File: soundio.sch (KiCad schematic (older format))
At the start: 13 parts, among them J3 PORT B, J4 PORT B, Q1 2N3904, U13 AY-3-8910, U14 LM741

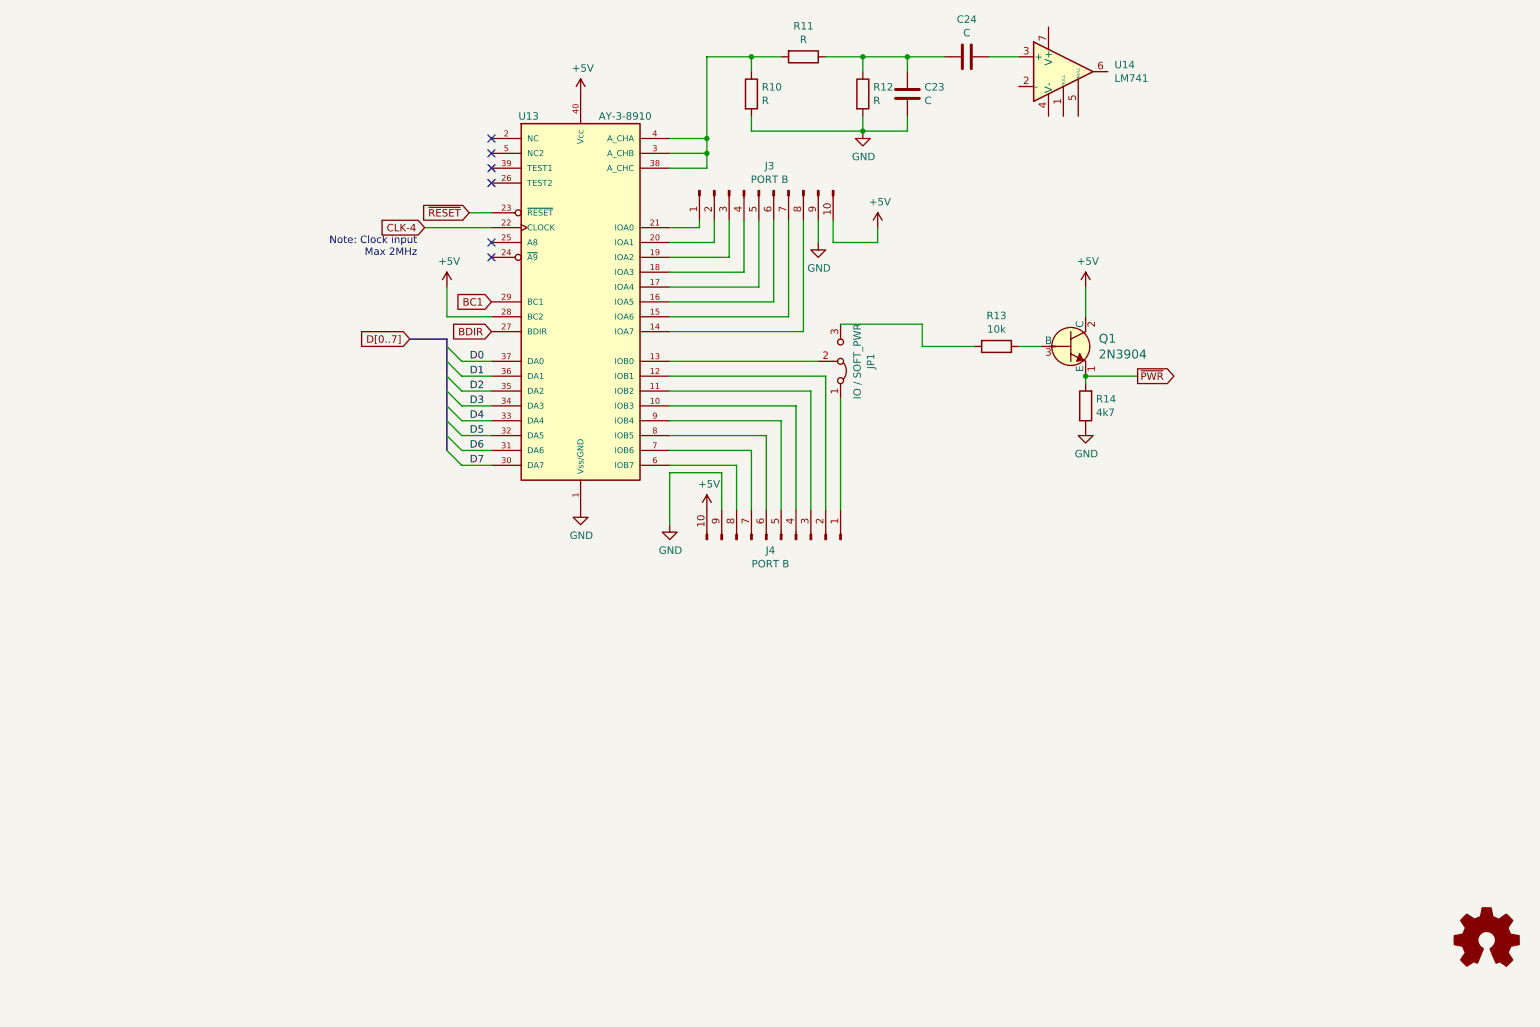
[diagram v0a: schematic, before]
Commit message: Added RTC
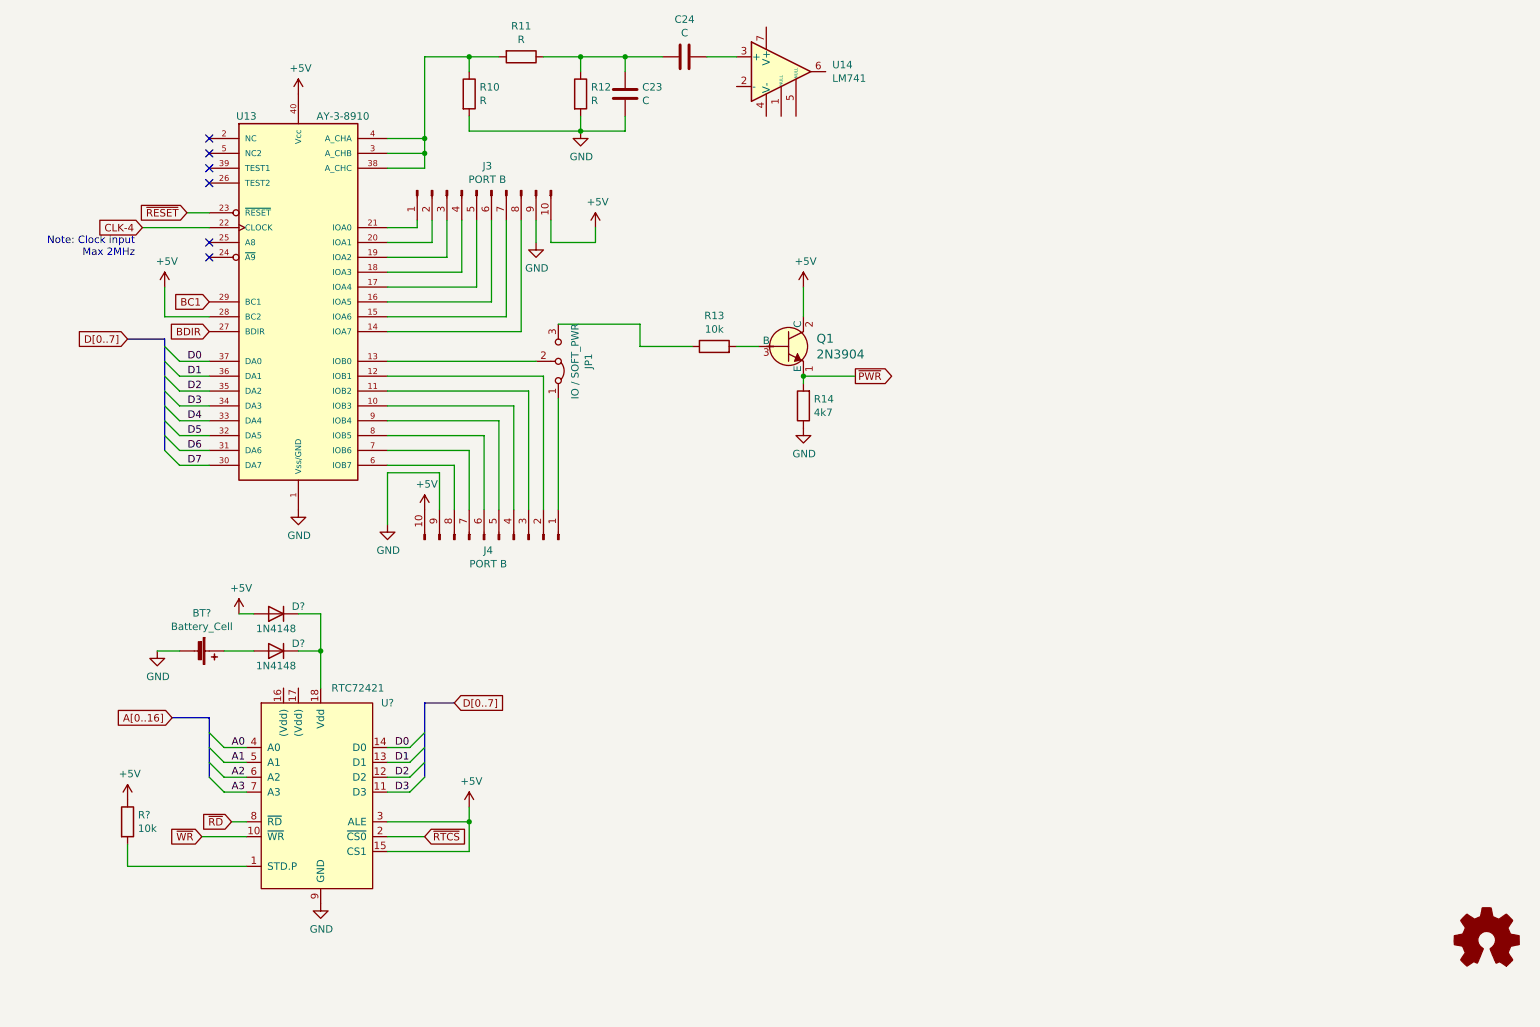
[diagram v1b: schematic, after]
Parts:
- added BT?: Battery_Cell, symbol Device:Battery_Cell
- added D? (x2): 1N4148, Diode_THT:D_DO-35_SOD27_P7.62mm_Horizontal, symbol Diode:1N4148
- added R?: 10k, symbol Device:R
- added U?: RTC72421, Package_DIP:DIP-18_W7.62mm_Socket_LongPads, symbol personal:RTC72421
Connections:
- net +5V: now also D?.2 (A), R?.1, U?.15 (CS1), U?.3 (ALE)
- net D0: now also U?.14 (D0)
- net D1: now also U?.13 (D1)
- net D2: now also U?.12 (D2)
- net D3: now also U?.11 (D3)
- net GND: now also BT?.2 (-), U?.9 (GND)
- new net: R?.2, U?.1 (STD.P)
- new net: D?.1 (K), D?.1 (K), U?.18 (Vdd)
- new net: BT?.1 (+), D?.2 (A)
- new net A0: U?.4 (A0)
- new net A1: U?.5 (A1)
- new net A2: U?.6 (A2)
- new net A3: U?.7 (A3)
- new net ~RD: U?.8 (~RD)
- new net ~RTCS: U?.2 (~CS0)
- new net ~WR: U?.10 (~WR)
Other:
- moved on the sheet: C23, C24, J3, J4, JP1, Q1, R10, R11, R12, R13, R14, U13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

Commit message: Added PSG audio output stage
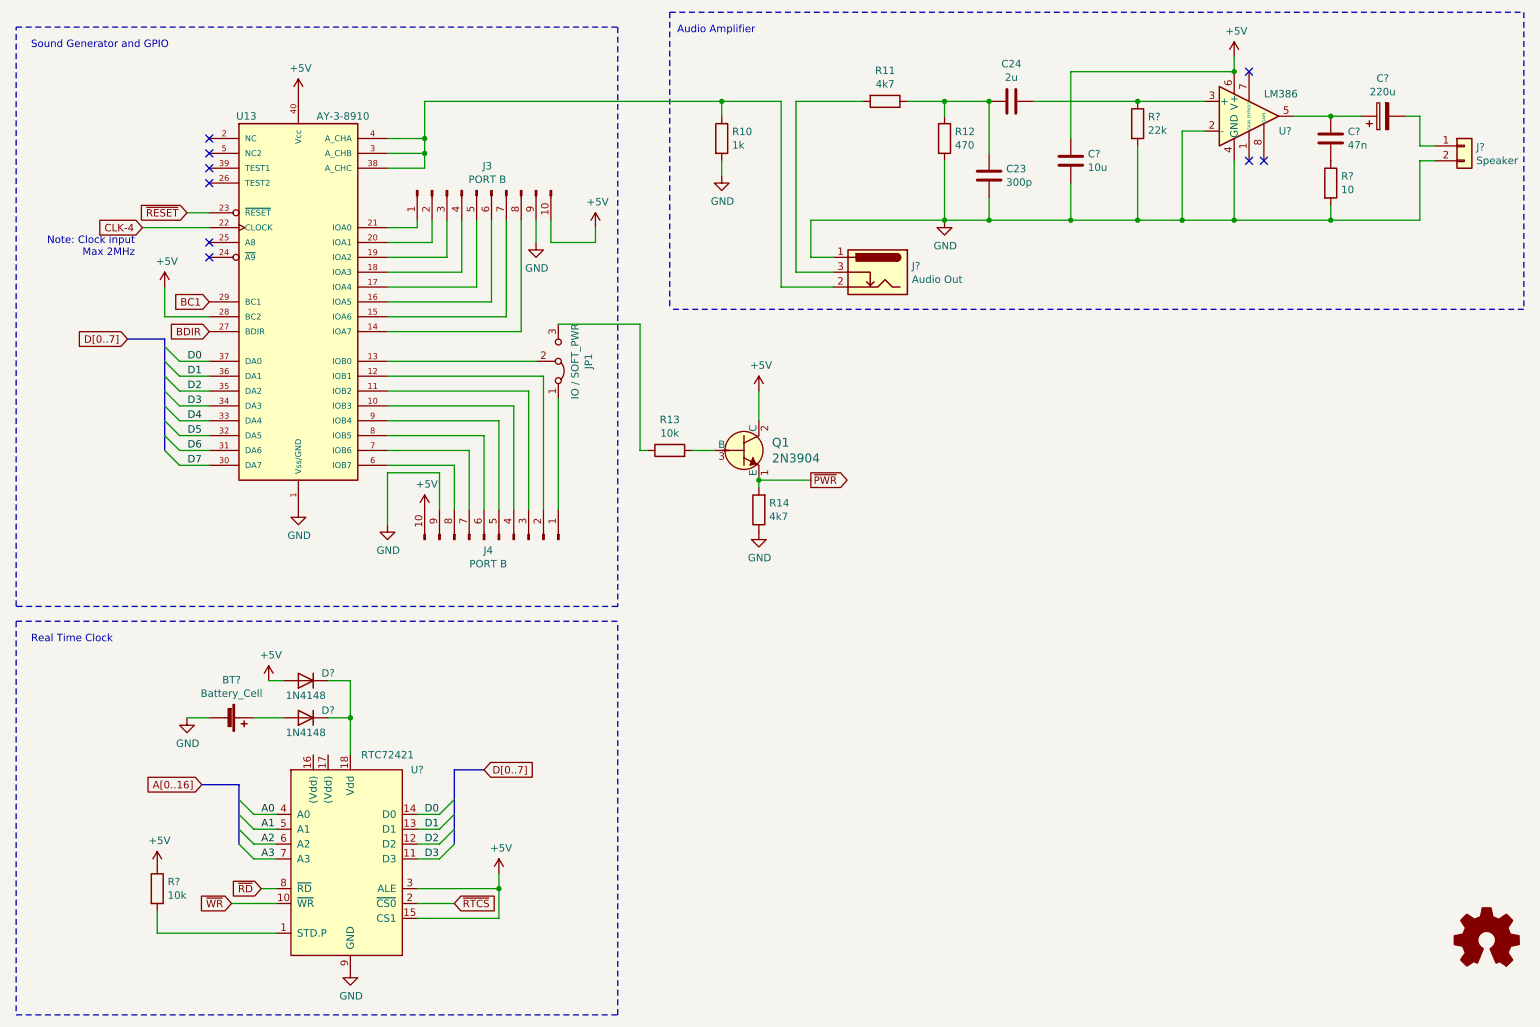
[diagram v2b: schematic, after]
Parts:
- removed U14: LM741, symbol Amplifier_Operational:LM741
- added C?: 220u, symbol Device:CP
- added C?: 47n, symbol Device:C
- added C?: 10u, symbol Device:C
- added J?: Speaker, symbol Connector_Generic:Conn_01x02
- added J?: Audio Out, symbol Connector:Barrel_Jack_Switch
- added R?: 22k, symbol Device:R
- added R?: 10, symbol Device:R
- added U?: LM386, symbol Amplifier_Audio:LM386
- C23: value C -> 300p
- C24: value C -> 2u
- R10: value R -> 1k
- R11: value R -> 4k7
- R12: value R -> 470
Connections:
- net +5V: now also C?.1, U?.6 (V+)
- net GND: now also C?.2, J?.1, J?.2 (Pin_2), R?.2, R?.2, U?.2 (-), U?.4 (GND)
- net at R10.1, U13.3 (A_CHB), U13.38 (A_CHC)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: now also J?.2; no longer R11.2
- net at C24.1: now also R?.1, U?.3 (+)
- new net: J?.3, R11.2
- new net: C?.1, C?.1, U?.5
- new net: C?.2, J?.1 (Pin_1)
- new net: C?.2, R?.1
- no-connect marks 6 -> 9
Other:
- note added: "Audio Amplifier"
- note added: "Real Time Clock"
- note added: "Sound Generator and GPIO"
- moved on the sheet: BT?, C23, C24, D?, Q1, R10, R11, R12, R13, R14, R?, U?
